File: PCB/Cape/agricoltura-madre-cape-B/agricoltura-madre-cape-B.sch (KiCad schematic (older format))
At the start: 0 parts

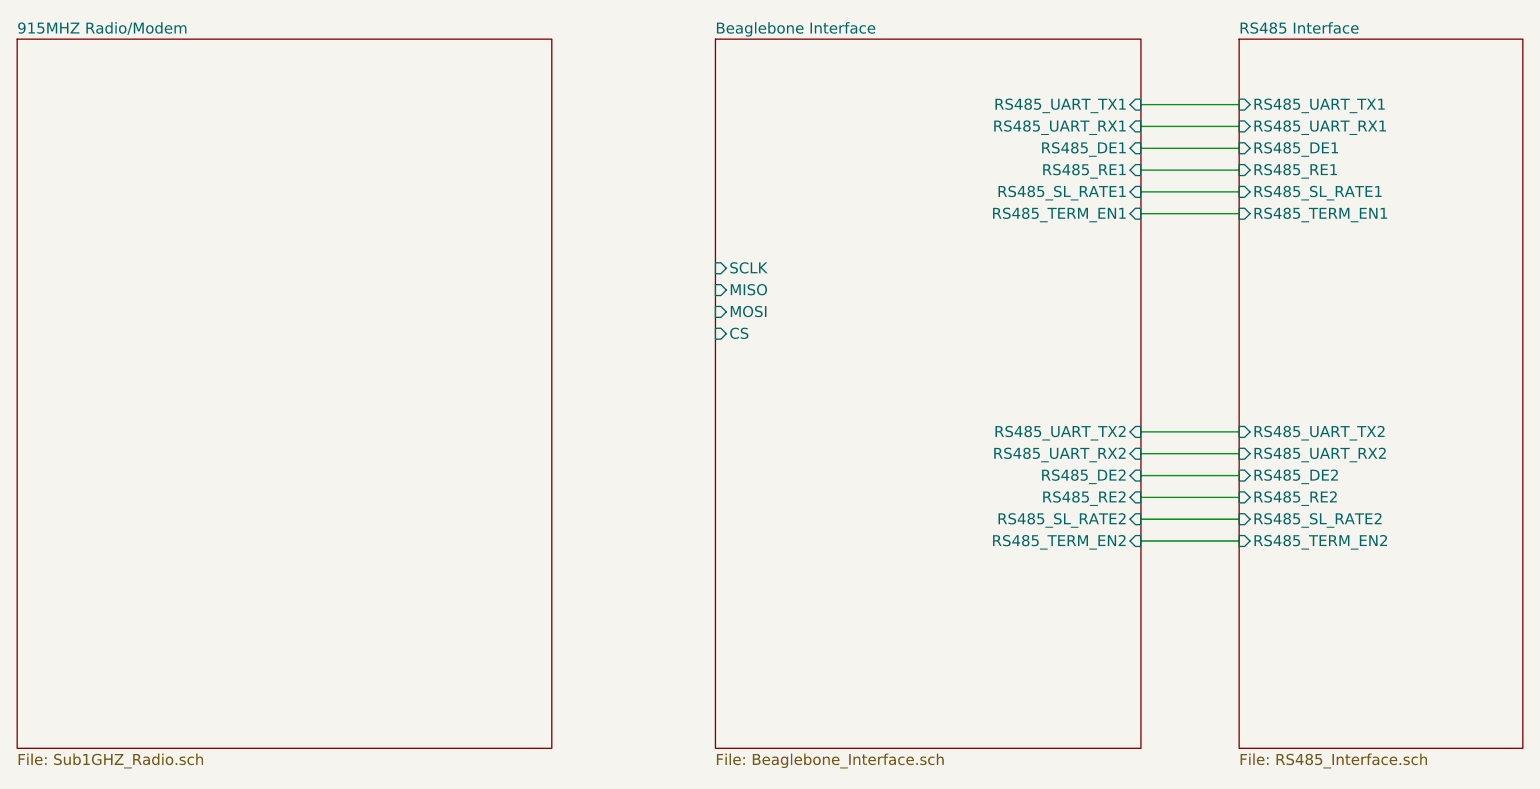
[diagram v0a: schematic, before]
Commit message: RPi4 Version and Cape Fork
Forked the Beaglebone Green Cape version of madre, there are now two variants, one with the SPI to 4 UART bridge and one without that will talk to all Radios/Modems via SPI directly using spare IO pins as chip selects.
RPi4 hat version created from a past project, performed all the basic modifications to the schematic to creat the pi version of madre, this one is the most developed version at the moment.
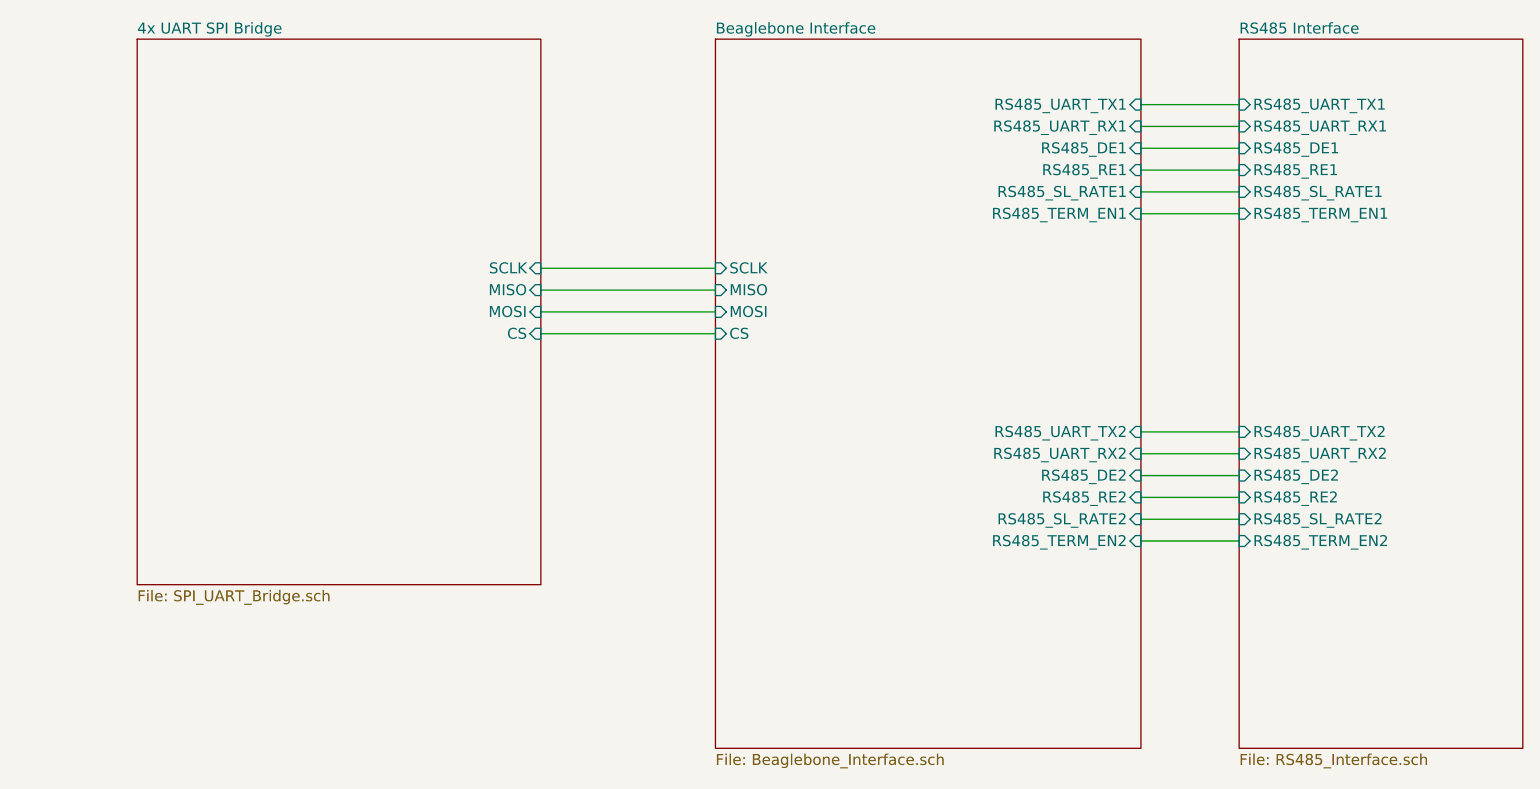
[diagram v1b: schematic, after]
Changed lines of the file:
@@
 	9250 4200 9700 4200
 $Sheet
-S 4100 1900 2450 3250
-U 5F03E6AE
-F0 "915MHZ Radio/Modem" 50
-F1 "Sub1GHZ_Radio.sch" 50
+S 4650 1900 1850 2500
+U 5EFE97F6
+F0 "4x UART SPI Bridge" 50
+F1 "SPI_UART_Bridge.sch" 50
+F2 "SCLK" I R 6500 2950 50
+F3 "MISO" I R 6500 3050 50
+F4 "MOSI" I R 6500 3150 50
+F5 "CS" I R 6500 3250 50
 $EndSheet
+Wire Wire Line
+	7300 3250 6500 3250
+Wire Wire Line
+	6500 3050 7300 3050
+Wire Wire Line
+	6500 3150 7300 3150
+Wire Wire Line
+	7300 2950 6500 2950
 $EndSCHEMATC
